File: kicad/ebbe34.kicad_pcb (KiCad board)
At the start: 2 copper layers, 250.3 x 111.4 mm, 90 parts, among them U2 nice_nano

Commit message: add power switch
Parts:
- added Bat+1: MountingHole_Pad, Library:Battery+, F.Cu at (169.3, 96.0)
- added Bat-1: MountingHole_Pad, Library:Battery-, F.Cu at (159.3, 95.5)
- added SW1: SW_SPDT, ScottoKeebs_Components:Switch_MSK12C02, B.Cu at (176.6, 82.2)
- moved D17 11.9 mm to (223.7, 91.9)
- moved S27 11.9 mm to (220.7, 108.3)
- moved D25 11.9 mm to (132.0, 121.5)
- moved D18 11.9 mm to (239.7, 83.3)
- moved S13 11.9 mm to (98.2, 83.6)
- moved REF** 11.9 mm to (270.9, 59.9)
- moved S11 11.9 mm to (58.5, 87.3)
- moved S14 11.9 mm to (114.2, 92.3)
- moved S19 11.9 mm to (249.2, 81.5)
- moved REF** 11.9 mm to (198.9, 130.3)
- moved S16 11.9 mm to (198.5, 99.9)
- moved S26 11.9 mm to (204.3, 115.9)
- moved D14 11.9 mm to (121.5, 97.9)
- moved D8 11.9 mm to (233.9, 67.3)
- moved D34 11.9 mm to (213.7, 137.9)
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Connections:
- U2 pad 24: unconnected-(U2-BATIN/P0.04-Pad24) -> RAW
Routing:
- net RAW: track 0.00 -> 29.0 mm
- net Bat+: track 0.00 -> 14.7 mm, vias 0 -> 1
- net GND: track 52.8 -> 58.5 mm

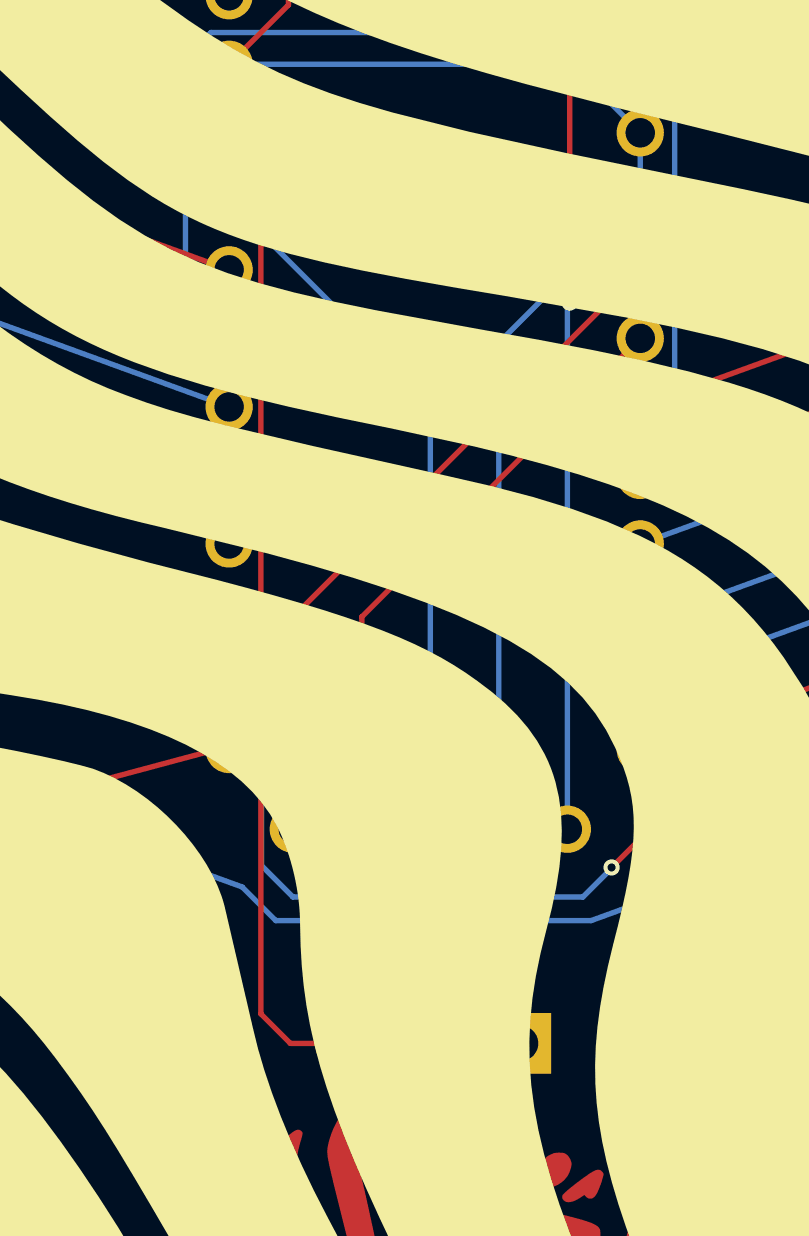
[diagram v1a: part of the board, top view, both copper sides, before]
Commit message: fix: move reset switch and tweak top plate
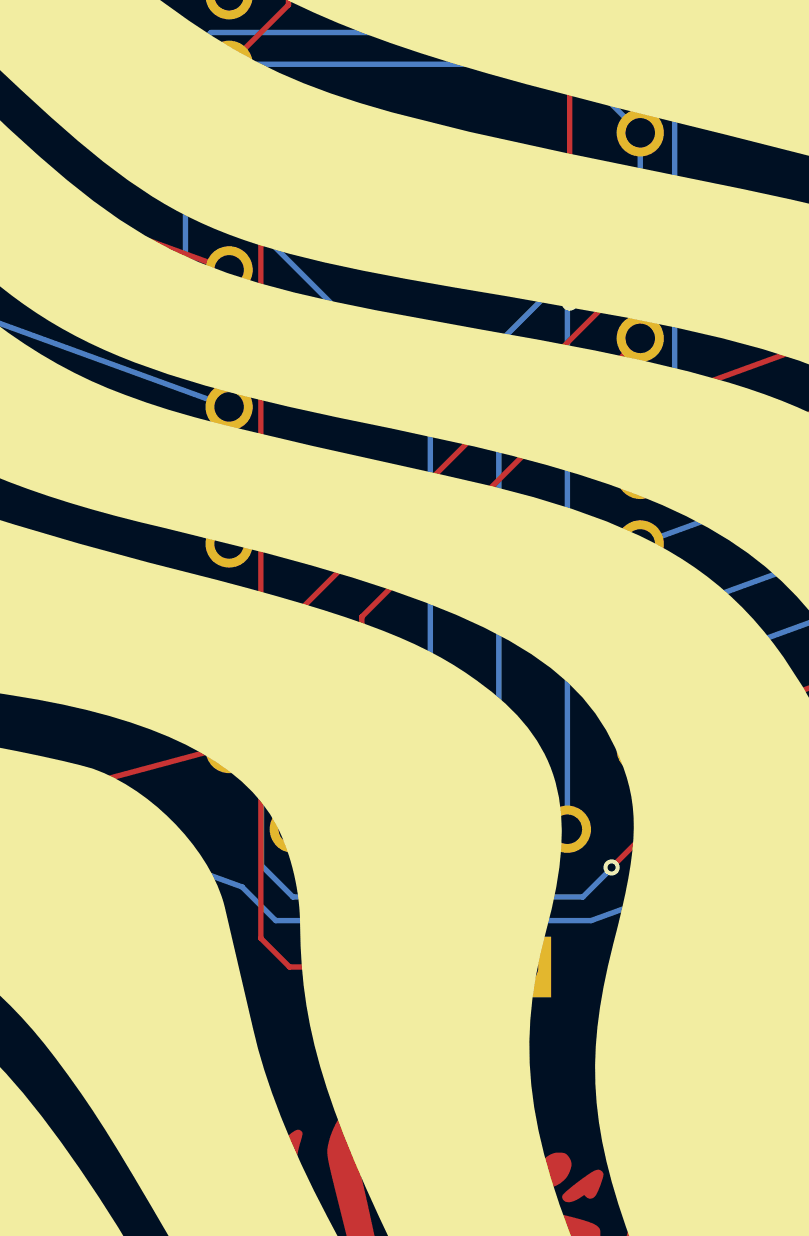
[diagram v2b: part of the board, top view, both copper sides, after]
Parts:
- moved RESET1 2.83 mm to (167.9, 133.9)
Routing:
- net GND: track 58.5 -> 55.7 mm
- net Reset: track 36.7 -> 33.9 mm
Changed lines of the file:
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@@
 	(footprint "ScottoKeebs_Components:Button_MJTP1243"
 		(layer "F.Cu")
-		(at 167.894697 136.705943 180)
+		(at 167.894697 133.875 180)
 		(descr "tactile push button, 6x3.5mm, https://www.apem.com/idec-apem/en_US/PCB-switches/Tactile-Switches/MJTP-6mm-through-hole/c/MJTP_6mm_through%20hole?page=1")
 		(tags "PHAP3362 6mm tact sw THT")
@@
 	)
 	(segment
-		(start 167.081633 128.768442)
-		(end 167.081626 135.892878)
+		(start 167.08163 133.061933)
+		(end 167.894697 133.875)
 		(width 0.2)
 		(layer "F.Cu")
@@
 	)
 	(segment
-		(start 167.081626 135.892878)
-		(end 167.894697 136.705943)
+		(start 159.283936 98.212463)
+		(end 157.083191 100.413206)
 		(width 0.2)
 		(layer "F.Cu")
@@
 	)
 	(segment
-		(start 159.283936 98.212463)
-		(end 157.083191 100.413206)
+		(start 167.08163 128.76845)
+		(end 167.08163 133.061933)
 		(width 0.2)
 		(layer "F.Cu")
@@
 	)
 	(segment
-		(start 161.394695 136.705946)
-		(end 159.353571 136.705946)
+		(start 161.394697 133.875)
+		(end 159.322986 133.875)
 		(width 0.2)
 		(layer "F.Cu")
@@
 	)
 	(segment
-		(start 159.353571 136.705946)
-		(end 158.260486 135.612858)
+		(start 159.322986 133.875)
+		(end 158.260486 132.8125)
 		(width 0.2)
 		(layer "F.Cu")
@@
 	)
 	(segment
-		(start 158.260486 135.612858)
+		(start 158.260486 132.8125)
 		(end 158.260481 104.130517)
 		(width 0.2)

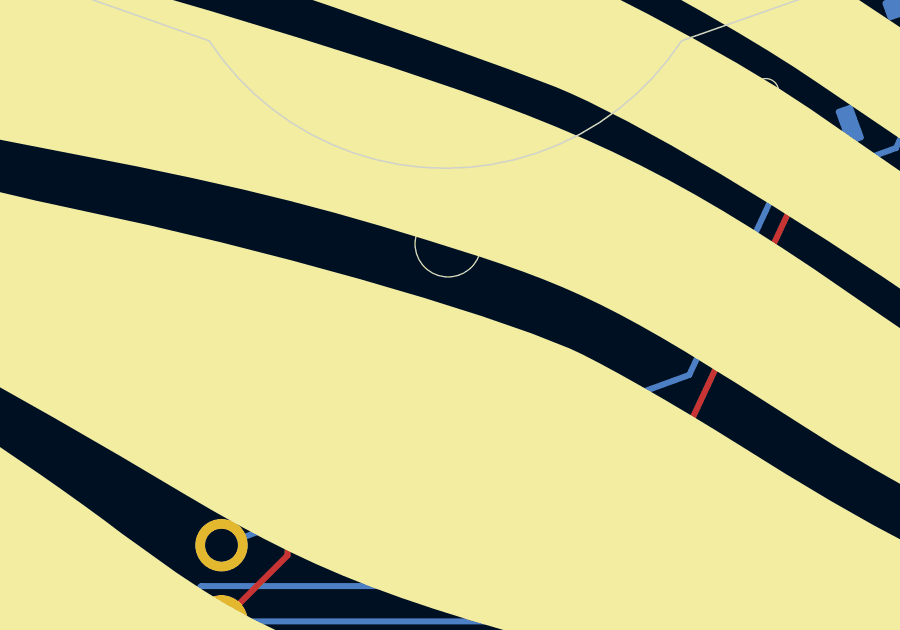
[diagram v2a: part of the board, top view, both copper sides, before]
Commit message: add screen cover
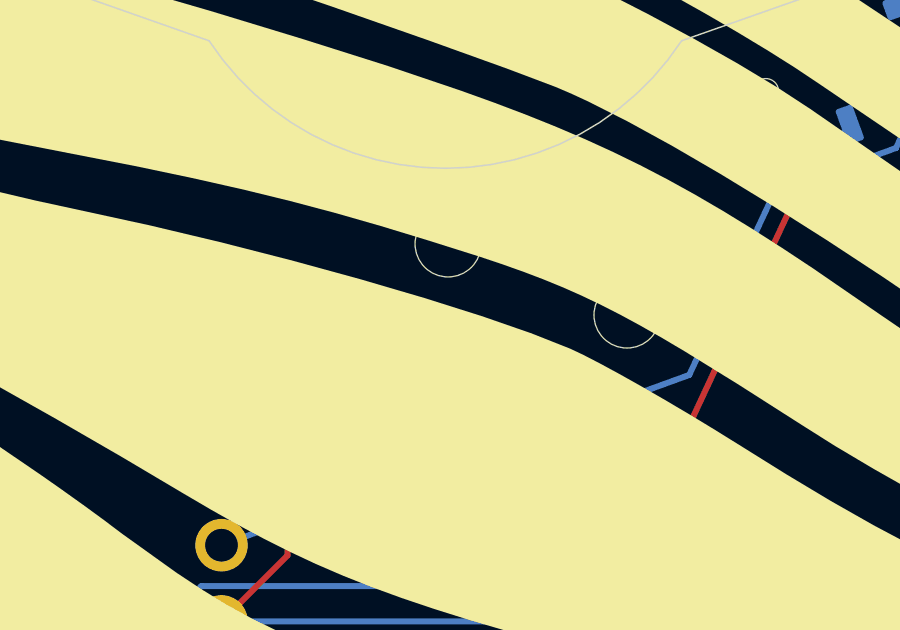
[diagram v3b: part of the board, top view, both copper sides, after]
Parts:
- added REF**: Standoff_M2x6mm, ScottoKeebs_Scotto:Standoff_M2x6mm, F.Cu at (158.8, 90.2)
- added REF**: Standoff_M2x6mm, ScottoKeebs_Scotto:Standoff_M2x6mm, F.Cu at (170.6, 90.2)
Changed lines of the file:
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@@
 		)
 	)
+	(footprint "ScottoKeebs_Scotto:Standoff_M2x6mm"
+		(layer "F.Cu")
+		(at 170.6 90.2)
+		(descr "Mounting Hole 2.2mm, no annular, M2")
+		(tags "mounting hole 2.2mm no annular m2")
+		(property "Reference" "REF**"
+			(at 0 -3.199999 0)
+			(layer "F.SilkS")
+			(hide yes)
+			(effects
+				(font
+					(size 1 1)
+					(thickness 0.15)
+				)
+			)
+		)
+		(property "Value" "Standoff_M2x6mm"
+			(at 0 3.199999 0)
+			(layer "F.Fab")
+			(hide yes)
+			(effects
+				(font
+					(size 1 1)
+					(thickness 0.15)
+				)
+			)
+		)
+		(property "Datasheet" ""
+			(at 0 0 0)
+			(unlocked yes)
+			(layer "F.Fab")
+			(hide yes)
+			(effects
+				(font
+					(size 1.27 1.27)
+					(thickness 0.15)
+				)
+			)
+		)
+		(property "Description" ""
+			(at 0 0 0)
+			(unlocked yes)
+			(layer "F.Fab")
+			(hide yes)
+			(effects
+				(font
+					(size 1.27 1.27)
+					(thickness 0.15)
+				)
+			)
+		)
+		(attr exclude_from_pos_files exclude_from_bom)
+		(fp_circle
+			(center 0 0)
+			(end 1.6 0)
+			(stroke
+				(width 0.05)
+				(type default)
+			)
+			(fill no)
+			(layer "B.CrtYd")
+		)
+		(pad "" np_thru_hole circle
+			(at 0 0)
+			(size 2.2 2.2)
+			(drill 2.2)
+			(layers "*.Cu" "*.Mask")
+		)
+		(embedded_fonts no)
+		(model "${SCOTTOKEEBS_KICAD}/3dmodels/ScottoKeebs_Scotto.3dshapes/Standoff.step"
+			(offset
+				(xyz 0 0 -7.6)
+			)
+			(scale
+				(xyz 1 1 6)
+			)
+			(rotate
+				(xyz 0 0 0)
+			)
+		)
+	)
 	(footprint "ScottoKeebs_Hotswap:Hotswap_Choc_V1V2"
 		(layer "F.Cu")
@@
 	)
 	(footprint "ScottoKeebs_Scotto:Standoff_M2x6mm"
+		(layer "F.Cu")
+		(at 158.8 90.2)
+		(descr "Mounting Hole 2.2mm, no annular, M2")
+		(tags "mounting hole 2.2mm no annular m2")
+		(property "Reference" "REF**"
+			(at 0 -3.199999 0)
+			(layer "F.SilkS")
+			(hide yes)
+			(effects
+				(font
+					(size 1 1)
+					(thickness 0.15)
+				)
+			)
+		)
+		(property "Value" "Standoff_M2x6mm"
+			(at 0 3.199999 0)
+			(layer "F.Fab")
+			(hide yes)
+			(effects
+				(font
+					(size 1 1)
+					(thickness 0.15)
+				)
+			)
+		)
+		(property "Datasheet" ""
+			(at 0 0 0)
+			(unlocked yes)
+			(layer "F.Fab")
+			(hide yes)
+			(effects
+				(font
+					(size 1.27 1.27)
+					(thickness 0.15)
+				)
+			)
+		)
+		(property "Description" ""
+			(at 0 0 0)
+			(unlocked yes)
+			(layer "F.Fab")
+			(hide yes)
+			(effects
+				(font
+					(size 1.27 1.27)
+					(thickness 0.15)
+				)
+			)
+		)
+		(attr exclude_from_pos_files exclude_from_bom)
+		(fp_circle
+			(center 0 0)
+			(end 1.6 0)
+			(stroke
+				(width 0.05)
+				(type default)
+			)
+			(fill no)
+			(layer "B.CrtYd")
+		)
+		(pad "" np_thru_hole circle
+			(at 0 0)
+			(size 2.2 2.2)
+			(drill 2.2)
+			(layers "*.Cu" "*.Mask")
+		)
+		(embedded_fonts no)
+		(model "${SCOTTOKEEBS_KICAD}/3dmodels/ScottoKeebs_Scotto.3dshapes/Standoff.step"
+			(offset
+				(xyz 0 0 -7.6)
+			)
+			(scale
+				(xyz 1 1 6)
+			)
+			(rotate
+				(xyz 0 0 0)
+			)
+		)
+	)
+	(footprint "ScottoKeebs_Scotto:Standoff_M2x6mm"
